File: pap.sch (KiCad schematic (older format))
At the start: 0 parts

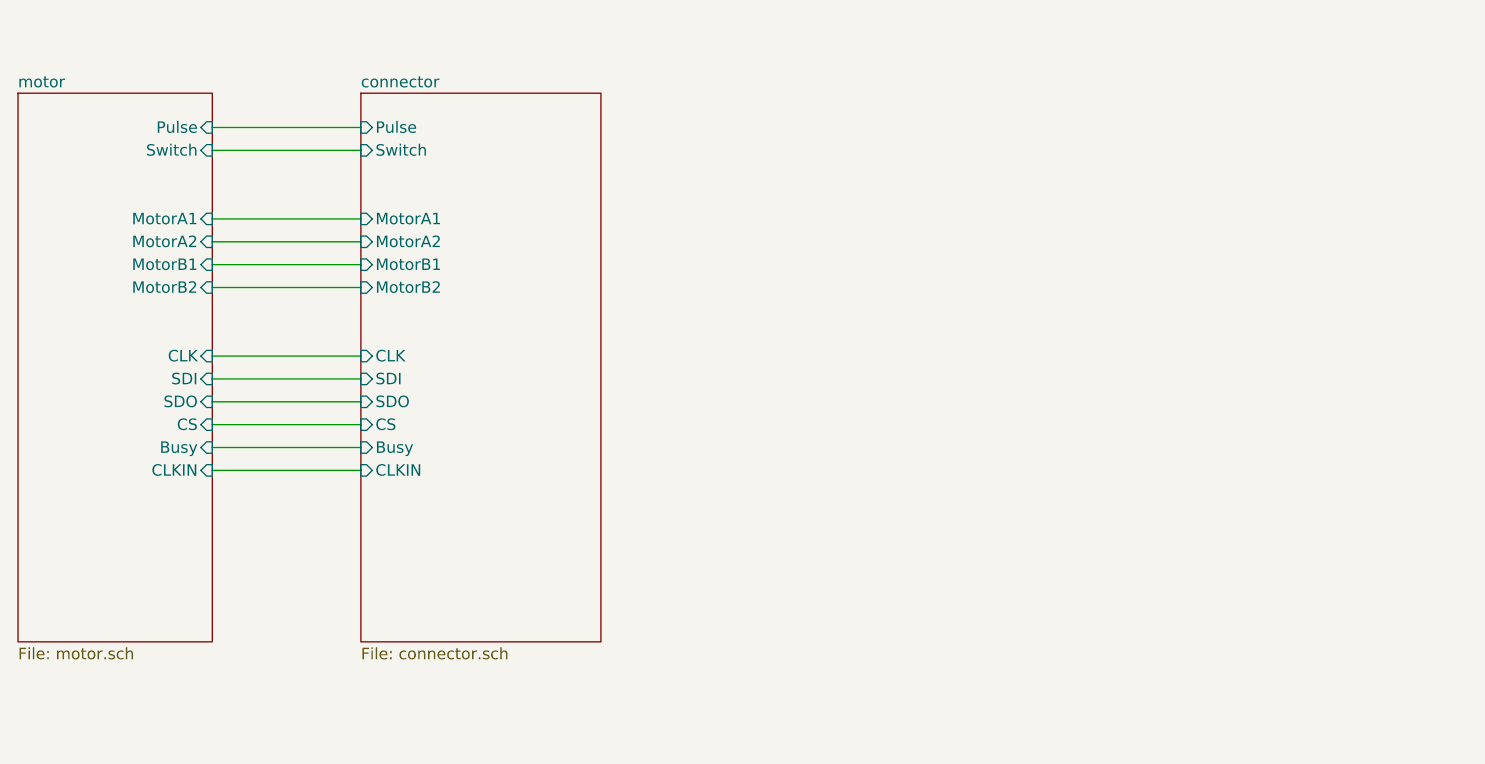
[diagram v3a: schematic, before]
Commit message: Cambio Rj's vuela xtal, entra Reset, agrego tornillos
Hago de todo un poco entre lo que saco el xtal porque ya probe que no se
necesita, elijo un IC que gnere 16Mhz y lo encadeno al resto, el RJ lo
cambie por otra que se parece mas a la que voy a usar, pero hay que
verificar, agregue un selector de osc, y agregue unos agujeros de
tornillos que no se si los quiero. va bien.. tengo que meterle mas al
ruteo
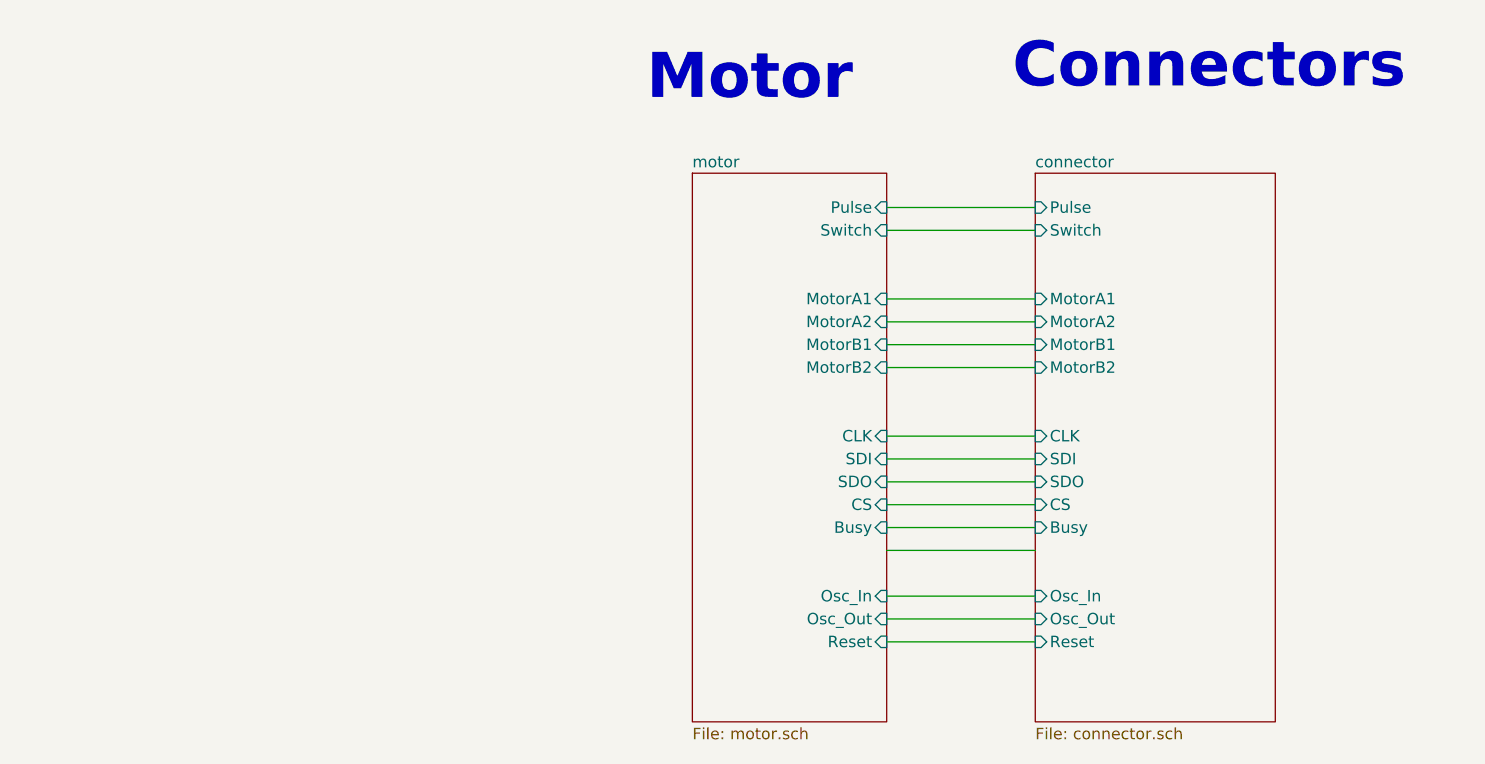
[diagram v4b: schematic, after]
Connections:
- wire segments 12 -> 15
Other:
- note added: "Connectors\n"
- note added: "Motor\n"
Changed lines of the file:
@@
 Comment4 ""
 $EndDescr
+Wire Wire Line
+	8150 4150 7500 4150
+Wire Wire Line
+	7500 4250 8150 4250
+Wire Wire Line
+	8150 4550 7500 4550
+Wire Wire Line
+	8150 4650 7500 4650
+Wire Wire Line
+	8150 4750 7500 4750
+Wire Wire Line
+	7500 4850 8150 4850
+Wire Wire Line
+	7500 5250 8150 5250
+Wire Wire Line
+	7500 5150 8150 5150
+Wire Wire Line
+	7500 5350 8150 5350
+Wire Wire Line
+	8150 5450 7500 5450
+Wire Wire Line
+	7500 5550 8150 5550
+Wire Wire Line
+	7500 5650 8150 5650
+Wire Wire Line
+	7500 5850 8150 5850
+Wire Wire Line
+	8150 5950 7500 5950
 $Sheet
-S 5200 3650 1050 2400
+S 6650 4000 850  2400
+U 5BA6E8FB
+F0 "motor" 50
+F1 "motor.sch" 50
+F2 "MotorA1" I R 7500 4550 50
+F3 "MotorA2" I R 7500 4650 50
+F4 "MotorB1" I R 7500 4750 50
+F5 "MotorB2" I R 7500 4850 50
+F6 "CS" I R 7500 5450 50
+F7 "SDI" I R 7500 5250 50
+F8 "SDO" I R 7500 5350 50
+F9 "Busy" I R 7500 5550 50
+F10 "Pulse" I R 7500 4150 50
+F11 "Switch" I R 7500 4250 50
+F12 "CLK" I R 7500 5150 50
+F13 "Osc_In" I R 7500 5850 50
+F14 "Osc_Out" I R 7500 5950 50
+F15 "Reset" I R 7500 6050 50
+$EndSheet
+$Sheet
+S 8150 4000 1050 2400
 U 5BA6E5CE
 F0 "connector" 50
 F1 "connector.sch" 50
-F2 "CS" I L 5200 5100 50
-F3 "CLK" I L 5200 4800 50
-F4 "SDI" I L 5200 4900 50
-F5 "Busy" I L 5200 5200 50
-F6 "Pulse" I L 5200 3800 50
-F7 "Switch" I L 5200 3900 50
-F8 "MotorB2" I L 5200 4500 50
-F9 "MotorA2" I L 5200 4300 50
-F10 "MotorA1" I L 5200 4200 50
-F11 "MotorB1" I L 5200 4400 50
-F12 "SDO" I L 5200 5000 50
-F13 "CLKIN" I L 5200 5300 50
+F2 "CS" I L 8150 5450 50
+F3 "CLK" I L 8150 5150 50
+F4 "SDI" I L 8150 5250 50
+F5 "Pulse" I L 8150 4150 50
+F6 "Switch" I L 8150 4250 50
+F7 "MotorB2" I L 8150 4850 50
+F8 "MotorA2" I L 8150 4650 50
+F9 "MotorA1" I L 8150 4550 50
+F10 "MotorB1" I L 8150 4750 50
+F11 "SDO" I L 8150 5350 50
+F12 "Busy" I L 8150 5550 50
+F13 "Osc_In" I L 8150 5850 50
+F14 "Osc_Out" I L 8150 5950 50
+F15 "Reset" I L 8150 6050 50
 $EndSheet
+Text Notes 6450 3700 0    197  ~ 39
+Motor\n
+Text Notes 8050 3650 0    197  ~ 39
+Connectors\n
 Wire Wire Line
-	5200 3800 4550 3800
-Wire Wire Line
-	4550 3900 5200 3900
-Wire Wire Line
-	5200 4200 4550 4200
-Wire Wire Line
-	5200 4300 4550 4300
-Wire Wire Line
-	5200 4400 4550 4400
-Wire Wire Line
-	4550 4500 5200 4500
-Wire Wire Line
-	4550 4900 5200 4900
-Wire Wire Line
-	4550 4800 5200 4800
-Wire Wire Line
-	4550 5000 5200 5000
-Wire Wire Line
-	5200 5100 4550 5100
-Wire Wire Line
-	4550 5200 5200 5200
-$Sheet
-S 3700 3650 850  2400
-U 5BA6E8FB
-F0 "motor" 50
-F1 "motor.sch" 50
-F2 "MotorA1" I R 4550 4200 50
-F3 "MotorA2" I R 4550 4300 50
-F4 "MotorB1" I R 4550 4400 50
-F5 "MotorB2" I R 4550 4500 50
-F6 "CS" I R 4550 5100 50
-F7 "CLK" I R 4550 4800 50
-F8 "SDI" I R 4550 4900 50
-F9 "SDO" I R 4550 5000 50
-F10 "Busy" I R 4550 5200 50
-F11 "Pulse" I R 4550 3800 50
-F12 "Switch" I R 4550 3900 50
-F13 "CLKIN" I R 4550 5300 50
-$EndSheet
-Wire Wire Line
-	4550 5300 5200 5300
+	7500 6050 8150 6050
 $EndSCHEMATC

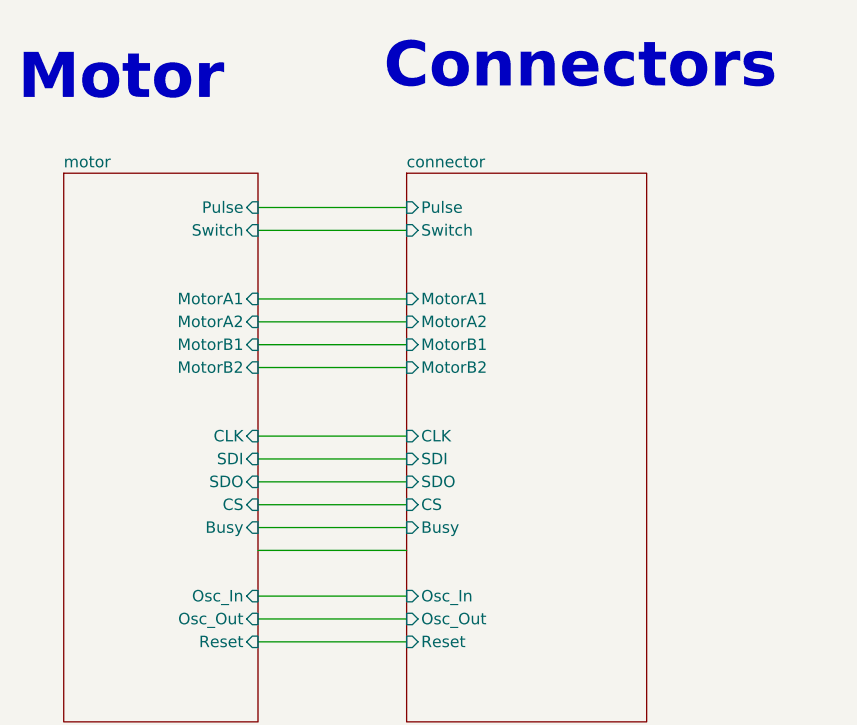
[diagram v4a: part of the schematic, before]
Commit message: cambio de nombres, mejorop serigrafia, agrego pin
agrego el pin de flag ya que me sobraba un pin en el RJ12, cambio los
nombres de 0-50 para motor y 51 a 100 para conector, ajusto el espesor
de la seri, y algunas cosas mas..
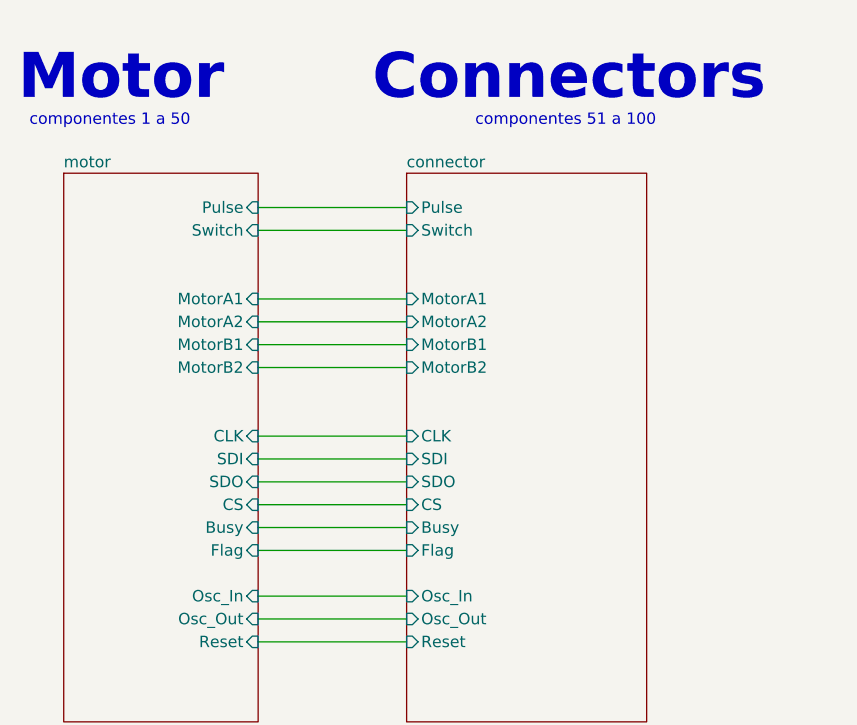
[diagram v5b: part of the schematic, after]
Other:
- note added: "componentes 1 a 50"
- note added: "componentes 51 a 100"
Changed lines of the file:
@@
 F14 "Osc_Out" I R 7500 5950 50
 F15 "Reset" I R 7500 6050 50
+F16 "Flag" I R 7500 5650 50
 $EndSheet
 $Sheet
@@
 F14 "Osc_Out" I L 8150 5950 50
 F15 "Reset" I L 8150 6050 50
+F16 "Flag" I L 8150 5650 50
 $EndSheet
 Text Notes 6450 3700 0    197  ~ 39
 Motor\n
-Text Notes 8050 3650 0    197  ~ 39
+Text Notes 8000 3700 0    197  ~ 39
 Connectors\n
 Wire Wire Line
 	7500 6050 8150 6050
+Text Notes 6500 3800 0    50   ~ 0
+componentes 1 a 50
+Text Notes 8450 3800 0    50   ~ 0
+componentes 51 a 100
 $EndSCHEMATC

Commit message: aghrego serigrafia, logos, faltan fiduciales aun
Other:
- note added: "Miscelaneous\n"
- note added: "componentes 101 a 151"
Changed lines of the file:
@@
 $Descr A3 16535 11693
 encoding utf-8
-Sheet 1 3
+Sheet 1 4
 Title "PaP"
 Date "2018-09-21"
@@
 $EndDescr
 Wire Wire Line
-	8150 4150 7500 4150
+	7650 2850 7000 2850
 Wire Wire Line
-	7500 4250 8150 4250
+	7000 2950 7650 2950
 Wire Wire Line
-	8150 4550 7500 4550
+	7650 3250 7000 3250
 Wire Wire Line
-	8150 4650 7500 4650
+	7650 3350 7000 3350
 Wire Wire Line
-	8150 4750 7500 4750
+	7650 3450 7000 3450
 Wire Wire Line
-	7500 4850 8150 4850
+	7000 3550 7650 3550
 Wire Wire Line
-	7500 5250 8150 5250
+	7000 3950 7650 3950
 Wire Wire Line
-	7500 5150 8150 5150
+	7000 3850 7650 3850
 Wire Wire Line
-	7500 5350 8150 5350
+	7000 4050 7650 4050
 Wire Wire Line
-	8150 5450 7500 5450
+	7650 4150 7000 4150
 Wire Wire Line
-	7500 5550 8150 5550
+	7000 4250 7650 4250
 Wire Wire Line
-	7500 5650 8150 5650
+	7000 4350 7650 4350
 Wire Wire Line
-	7500 5850 8150 5850
+	7000 4550 7650 4550
 Wire Wire Line
-	8150 5950 7500 5950
+	7650 4650 7000 4650
 $Sheet
-S 6650 4000 850  2400
+S 6150 2700 850  2400
 U 5BA6E8FB
 F0 "motor" 50
 F1 "motor.sch" 50
-F2 "MotorA1" I R 7500 4550 50
-F3 "MotorA2" I R 7500 4650 50
-F4 "MotorB1" I R 7500 4750 50
-F5 "MotorB2" I R 7500 4850 50
-F6 "CS" I R 7500 5450 50
-F7 "SDI" I R 7500 5250 50
-F8 "SDO" I R 7500 5350 50
-F9 "Busy" I R 7500 5550 50
-F10 "Pulse" I R 7500 4150 50
-F11 "Switch" I R 7500 4250 50
-F12 "CLK" I R 7500 5150 50
-F13 "Osc_In" I R 7500 5850 50
-F14 "Osc_Out" I R 7500 5950 50
-F15 "Reset" I R 7500 6050 50
-F16 "Flag" I R 7500 5650 50
+F2 "MotorA1" I R 7000 3250 50
+F3 "MotorA2" I R 7000 3350 50
+F4 "MotorB1" I R 7000 3450 50
+F5 "MotorB2" I R 7000 3550 50
+F6 "CS" I R 7000 4150 50
+F7 "SDI" I R 7000 3950 50
+F8 "SDO" I R 7000 4050 50
+F9 "Busy" I R 7000 4250 50
+F10 "Pulse" I R 7000 2850 50
+F11 "Switch" I R 7000 2950 50
+F12 "CLK" I R 7000 3850 50
+F13 "Osc_In" I R 7000 4550 50
+F14 "Osc_Out" I R 7000 4650 50
+F15 "Reset" I R 7000 4750 50
+F16 "Flag" I R 7000 4350 50
 $EndSheet
 $Sheet
-S 8150 4000 1050 2400
+S 7650 2700 1050 2400
 U 5BA6E5CE
 F0 "connector" 50
 F1 "connector.sch" 50
-F2 "CS" I L 8150 5450 50
-F3 "CLK" I L 8150 5150 50
-F4 "SDI" I L 8150 5250 50
-F5 "Pulse" I L 8150 4150 50
-F6 "Switch" I L 8150 4250 50
-F7 "MotorB2" I L 8150 4850 50
-F8 "MotorA2" I L 8150 4650 50
-F9 "MotorA1" I L 8150 4550 50
-F10 "MotorB1" I L 8150 4750 50
-F11 "SDO" I L 8150 5350 50
-F12 "Busy" I L 8150 5550 50
-F13 "Osc_In" I L 8150 5850 50
-F14 "Osc_Out" I L 8150 5950 50
-F15 "Reset" I L 8150 6050 50
-F16 "Flag" I L 8150 5650 50
+F2 "CS" I L 7650 4150 50
+F3 "CLK" I L 7650 3850 50
+F4 "SDI" I L 7650 3950 50
+F5 "Pulse" I L 7650 2850 50
+F6 "Switch" I L 7650 2950 50
+F7 "MotorB2" I L 7650 3550 50
+F8 "MotorA2" I L 7650 3350 50
+F9 "MotorA1" I L 7650 3250 50
+F10 "MotorB1" I L 7650 3450 50
+F11 "SDO" I L 7650 4050 50
+F12 "Busy" I L 7650 4250 50
+F13 "Osc_In" I L 7650 4550 50
+F14 "Osc_Out" I L 7650 4650 50
+F15 "Reset" I L 7650 4750 50
+F16 "Flag" I L 7650 4350 50
 $EndSheet
-Text Notes 6450 3700 0    197  ~ 39
+Text Notes 5950 2400 0    197  ~ 39
 Motor\n
-Text Notes 8000 3700 0    197  ~ 39
+Text Notes 7500 2400 0    197  ~ 39
 Connectors\n
 Wire Wire Line
-	7500 6050 8150 6050
-Text Notes 6500 3800 0    50   ~ 0
+	7000 4750 7650 4750
+Text Notes 6000 2500 0    50   ~ 0
 componentes 1 a 50
-Text Notes 8450 3800 0    50   ~ 0
+Text Notes 7950 2500 0    50   ~ 0
 componentes 51 a 100
+$Sheet
+S 9950 2700 900  1050
+U 5BD8E387
+F0 "misc" 50
+F1 "misc.sch" 50
+$EndSheet
+Text Notes 9500 2450 0    197  ~ 39
+Miscelaneous\n
+Text Notes 9950 2550 0    50   ~ 0
+componentes 101 a 151
 $EndSCHEMATC

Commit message: voy terminando, me falta sacar los gerbers.. a por ellos...
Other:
- note added: "TP Final CESE2018\nPablo Slavkin\nDriver Motor Paso a Paso"
